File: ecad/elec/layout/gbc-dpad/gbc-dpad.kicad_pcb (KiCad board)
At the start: 2 copper layers, 225.7 x 100.8 mm, 0 parts

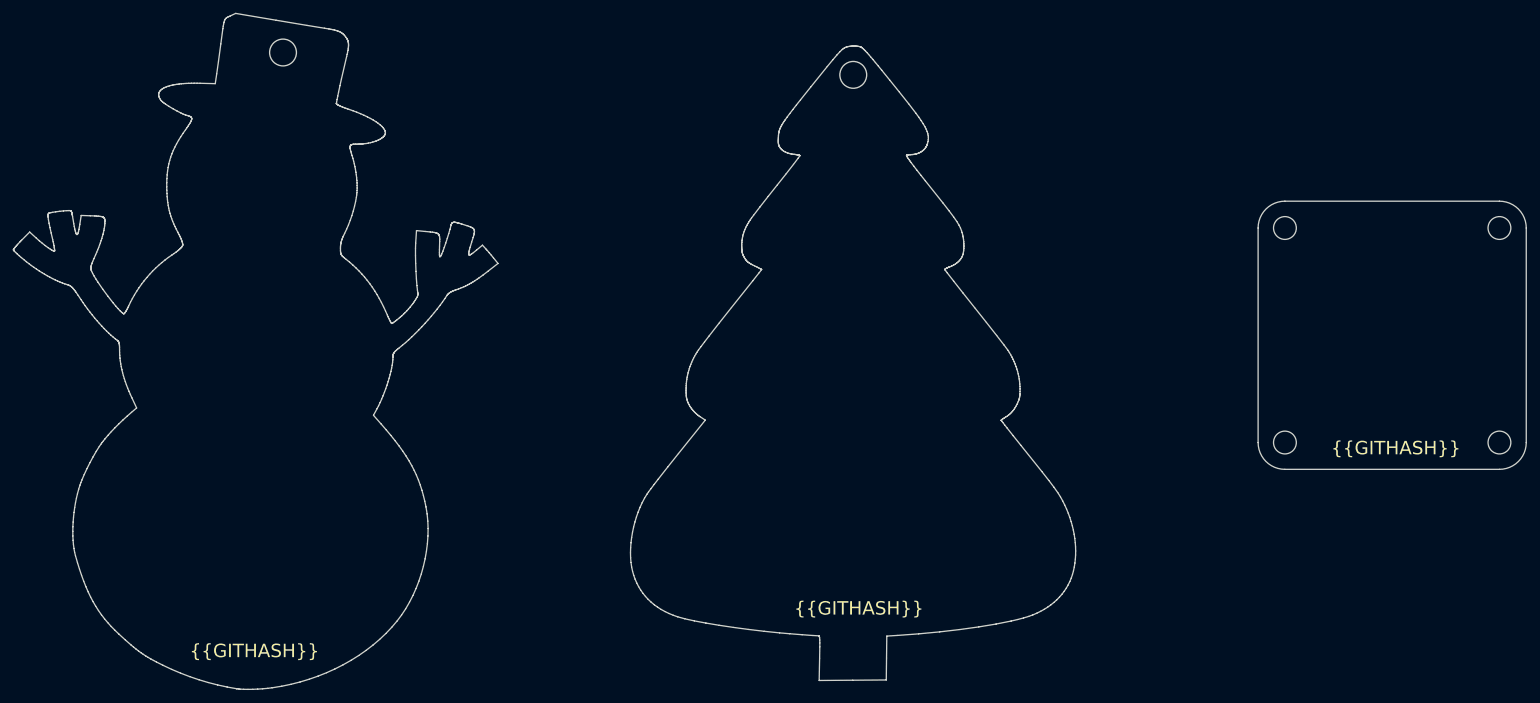
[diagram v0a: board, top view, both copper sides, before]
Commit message: WIP fleshing out and redoing some of the design to add some footprints / components for slik / membranes / etc.
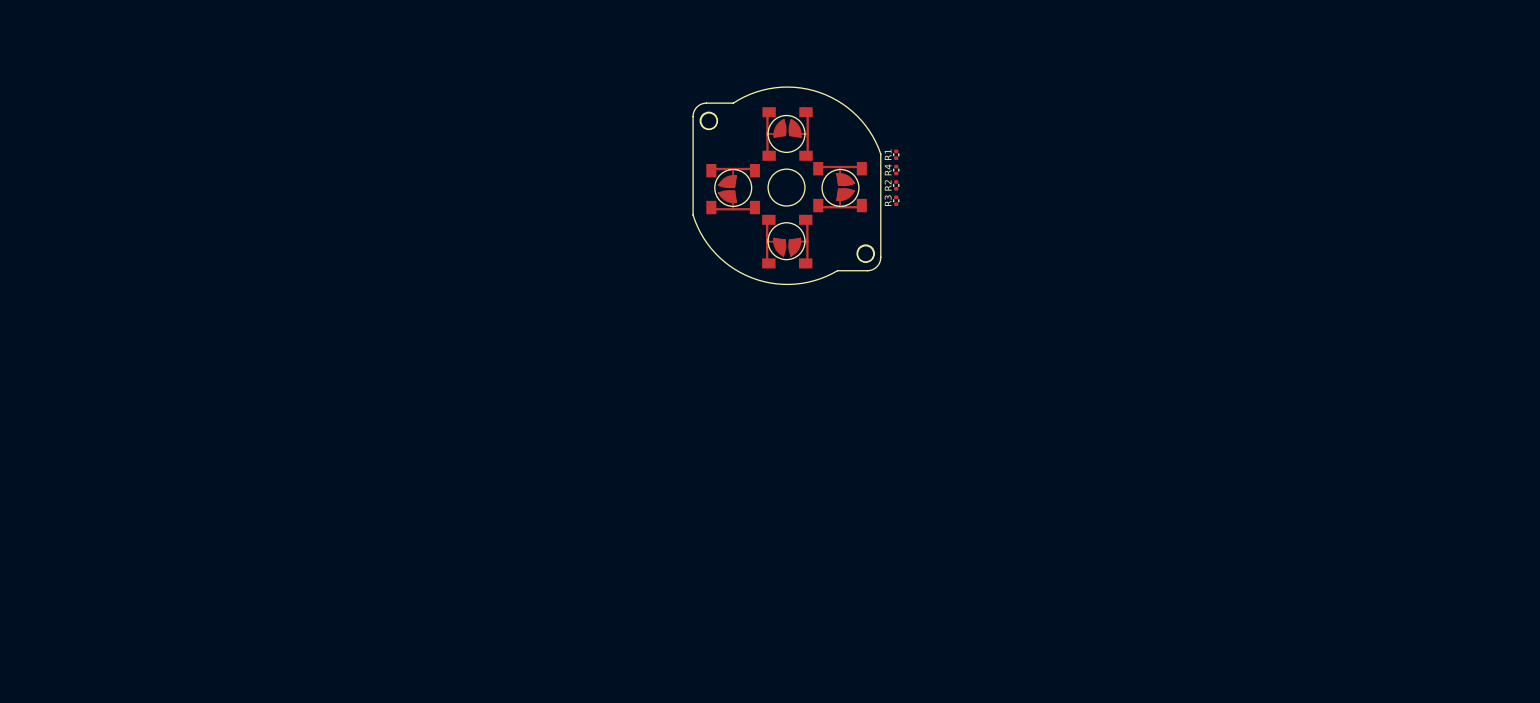
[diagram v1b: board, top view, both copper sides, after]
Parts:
- added R1: 62.5mW Thick Film Resistors 50V ±100ppm/℃ ±1% 10kΩ 0402 Chi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, lib:R0402, F.Cu at (167.6, 70.9)
- added R2: 62.5mW Thick Film Resistors 50V ±100ppm/℃ ±1% 10kΩ 0402 Chi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, lib:R0402, F.Cu at (167.6, 75.4)
- added R3: 62.5mW Thick Film Resistors 50V ±100ppm/℃ ±1% 10kΩ 0402 Chi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, lib:R0402, F.Cu at (167.6, 77.7)
- added R4: 62.5mW Thick Film Resistors 50V ±100ppm/℃ ±1% 10kΩ 0402 Chi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, lib:R0402, F.Cu at (167.6, 73.2)
- added U1: , lib:GAMEBOY_COLOR_DPAD_MEMBRANE, F.Cu at (151.3, 75.7)
- added U2: , lib:GBC_DPAD_BUTTON, F.Cu at (151.4, 67.8)
- added U3: , lib:GBC_DPAD_BUTTON, F.Cu at (151.4, 83.8)
- added U4: , lib:GBC_DPAD_BUTTON, F.Cu at (143.3, 76.0)
- added U5: , lib:GBC_DPAD_BUTTON, F.Cu at (159.3, 75.7)
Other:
- board outline removed
- board text removed: "{{GITHASH}}"
